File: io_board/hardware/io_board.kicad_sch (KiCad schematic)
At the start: 15 parts, among them J1 8bit_thing_bus_connector, J2 greenpak_i2c, J3 greenpak_i2c, J4 Micro_SD_Card_Det1, U1 SLG46826G, U2 W65C22, U3 74HCT164, U4 SLG46826G, U5 TLV73333PDBV

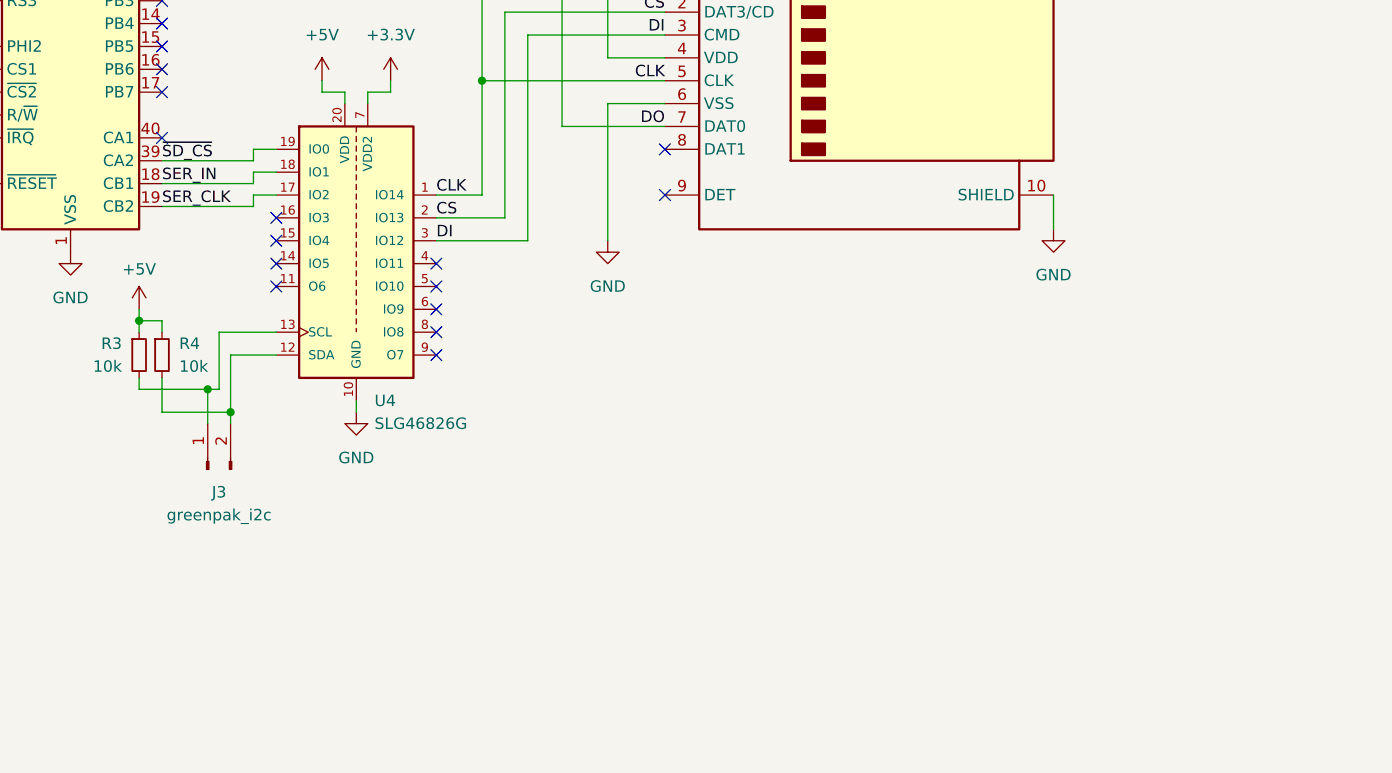
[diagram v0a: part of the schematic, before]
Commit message: Update IO board schematic and check in the necessary GreenPAK files
The io_spi_delay is built for a breadboard version using a '595 instead of a
'164, see the note in the schematic. It has an additional (further) delayed
clock line for the '595 register clock so we can shift and present the data in
the same PHI2 cycle.
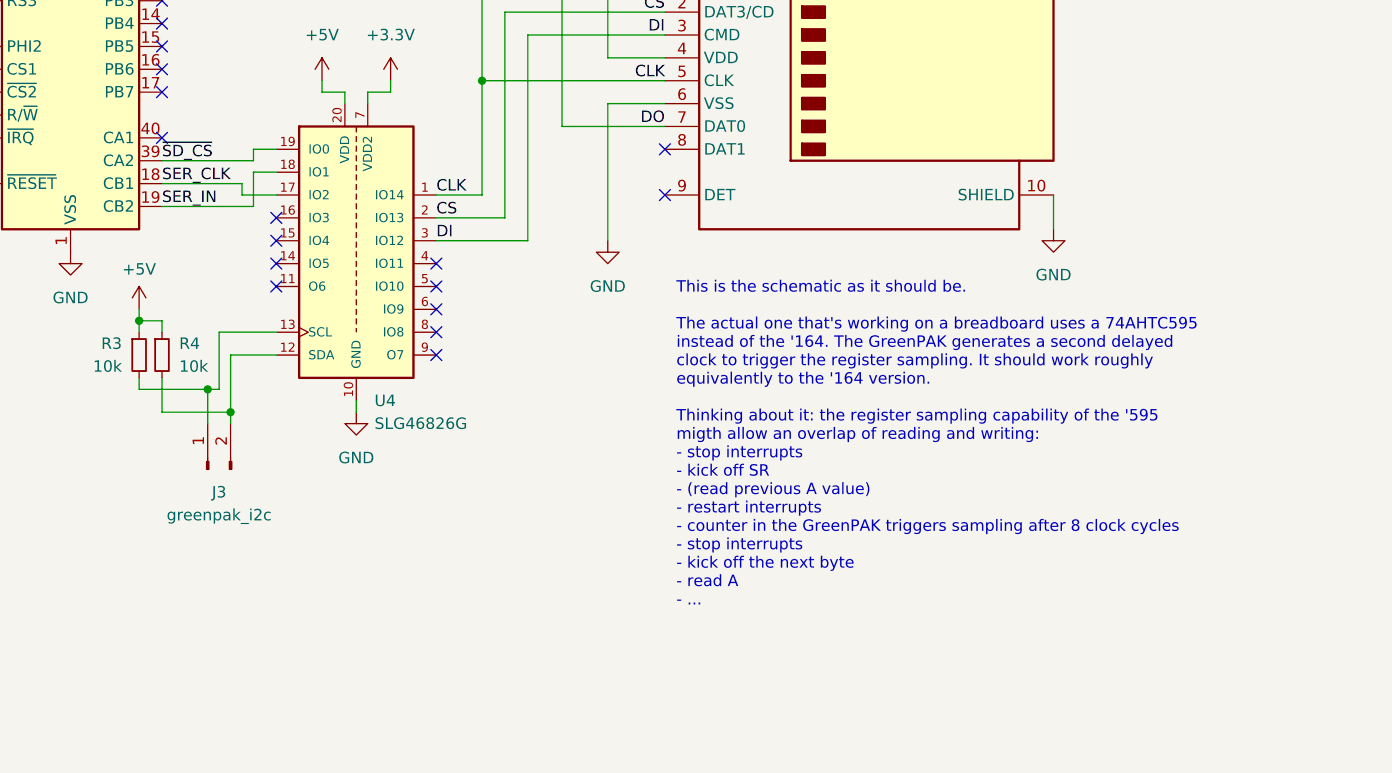
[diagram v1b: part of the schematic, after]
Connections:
- net SER_CLK: now also U2.18 (CB1); no longer U2.19 (CB2)
- net SER_IN: now also U2.19 (CB2); no longer U2.18 (CB1)
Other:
- note added: "This is the schematic as it should be. The actual one that's working on a breadboard uses a 74AHTC595 instead of the '164. The GreenPAK generates a second delayed clock to trigger the register sampling. It should work roughly equivalently to the '164 version. Thinking about it: the register sampling capability of the '595 migth allow an overlap of reading and writing: - stop interrupts - kick off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"
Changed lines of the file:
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@@
+	(wire
+		(pts
+			(xy 154.94 104.14) (xy 151.13 104.14)
+		)
+		(stroke
+			(width 0)
+			(type default)
+		)
+	)
 	(wire
 		(pts
@@
 	(wire
 		(pts
+			(xy 151.13 102.87) (xy 142.24 102.87)
+		)
+		(stroke
+			(width 0)
+			(type default)
+		)
+	)
+	(wire
+		(pts
 			(xy 53.34 138.43) (xy 53.34 139.7)
 		)
@@
 	(wire
 		(pts
-			(xy 142.24 102.87) (xy 152.4 102.87)
-		)
-		(stroke
-			(width 0)
-			(type default)
-		)
-	)
-	(wire
-		(pts
-			(xy 152.4 104.14) (xy 154.94 104.14)
-		)
-		(stroke
-			(width 0)
-			(type default)
-		)
-	)
-	(wire
-		(pts
 			(xy 220.98 44.45) (xy 220.98 40.64)
 		)
@@
 	(wire
 		(pts
-			(xy 152.4 105.41) (xy 152.4 104.14)
-		)
-		(stroke
-			(width 0)
-			(type default)
-		)
-	)
-	(wire
-		(pts
 			(xy 45.72 44.45) (xy 45.72 45.72)
 		)
@@
 	(wire
 		(pts
-			(xy 152.4 102.87) (xy 152.4 101.6)
+			(xy 151.13 104.14) (xy 151.13 102.87)
 		)
 		(stroke
@@
 	(wire
 		(pts
+			(xy 152.4 101.6) (xy 152.4 105.41)
+		)
+		(stroke
+			(width 0)
+			(type default)
+		)
+	)
+	(wire
+		(pts
 			(xy 167.64 92.71) (xy 165.1 92.71)
 		)
@@
 	(wire
 		(pts
-			(xy 152.4 101.6) (xy 154.94 101.6)
-		)
-		(stroke
-			(width 0)
-			(type default)
-		)
-	)
-	(wire
-		(pts
 			(xy 99.06 99.06) (xy 99.06 100.33)
 		)
@@
 	(wire
 		(pts
+			(xy 154.94 101.6) (xy 152.4 101.6)
+		)
+		(stroke
+			(width 0)
+			(type default)
+		)
+	)
+	(wire
+		(pts
 			(xy 182.88 86.36) (xy 182.88 109.22)
 		)
@@
 			(width 0)
 			(type default)
+		)
+	)
+	(text "This is the schematic as it should be.\n\nThe actual one that's working on a breadboard uses a 74AHTC595\ninstead of the '164. The GreenPAK generates a second delayed\nclock to trigger the register sampling. It should work roughly\nequivalently to the '164 version.\n\nThinking about it: the register sampling capability of the '595\nmigth allow an overlap of reading and writing:\n- stop interrupts\n- kick off SR\n- (read previous A value)\n- restart interrupts\n- counter in the GreenPAK triggers sampling after 8 clock cycles\n- stop interrupts\n- kick off the next byte\n- read A\n- ..."
+		(exclude_from_sim no)
+		(at 199.39 113.792 0)
+		(effects
+			(font
+				(size 1.27 1.27)
+			)
+			(justify left top)
 		)
 	)
@@
 	)
 	(label "SER_IN"
-		(at 142.24 102.87 0)
+		(at 142.24 105.41 0)
 		(fields_autoplaced yes)
 		(effects
@@
 		)
 	)
+	(label "SER_CLK"
+		(at 142.24 102.87 0)
+		(fields_autoplaced yes)
+		(effects
+			(font
+				(size 1.27 1.27)
+			)
+			(justify left bottom)
+		)
+	)
 	(label "CLK"
 		(at 121.92 87.63 180)
@@
 		(fields_autoplaced yes)
 		(effects
-			(font
-				(size 1.27 1.27)
-			)
-			(justify left bottom)
-		)
-	)
-	(label "SER_CLK"
-		(at 142.24 105.41 0)
-		(fields_autoplaced yes)
-		(effects

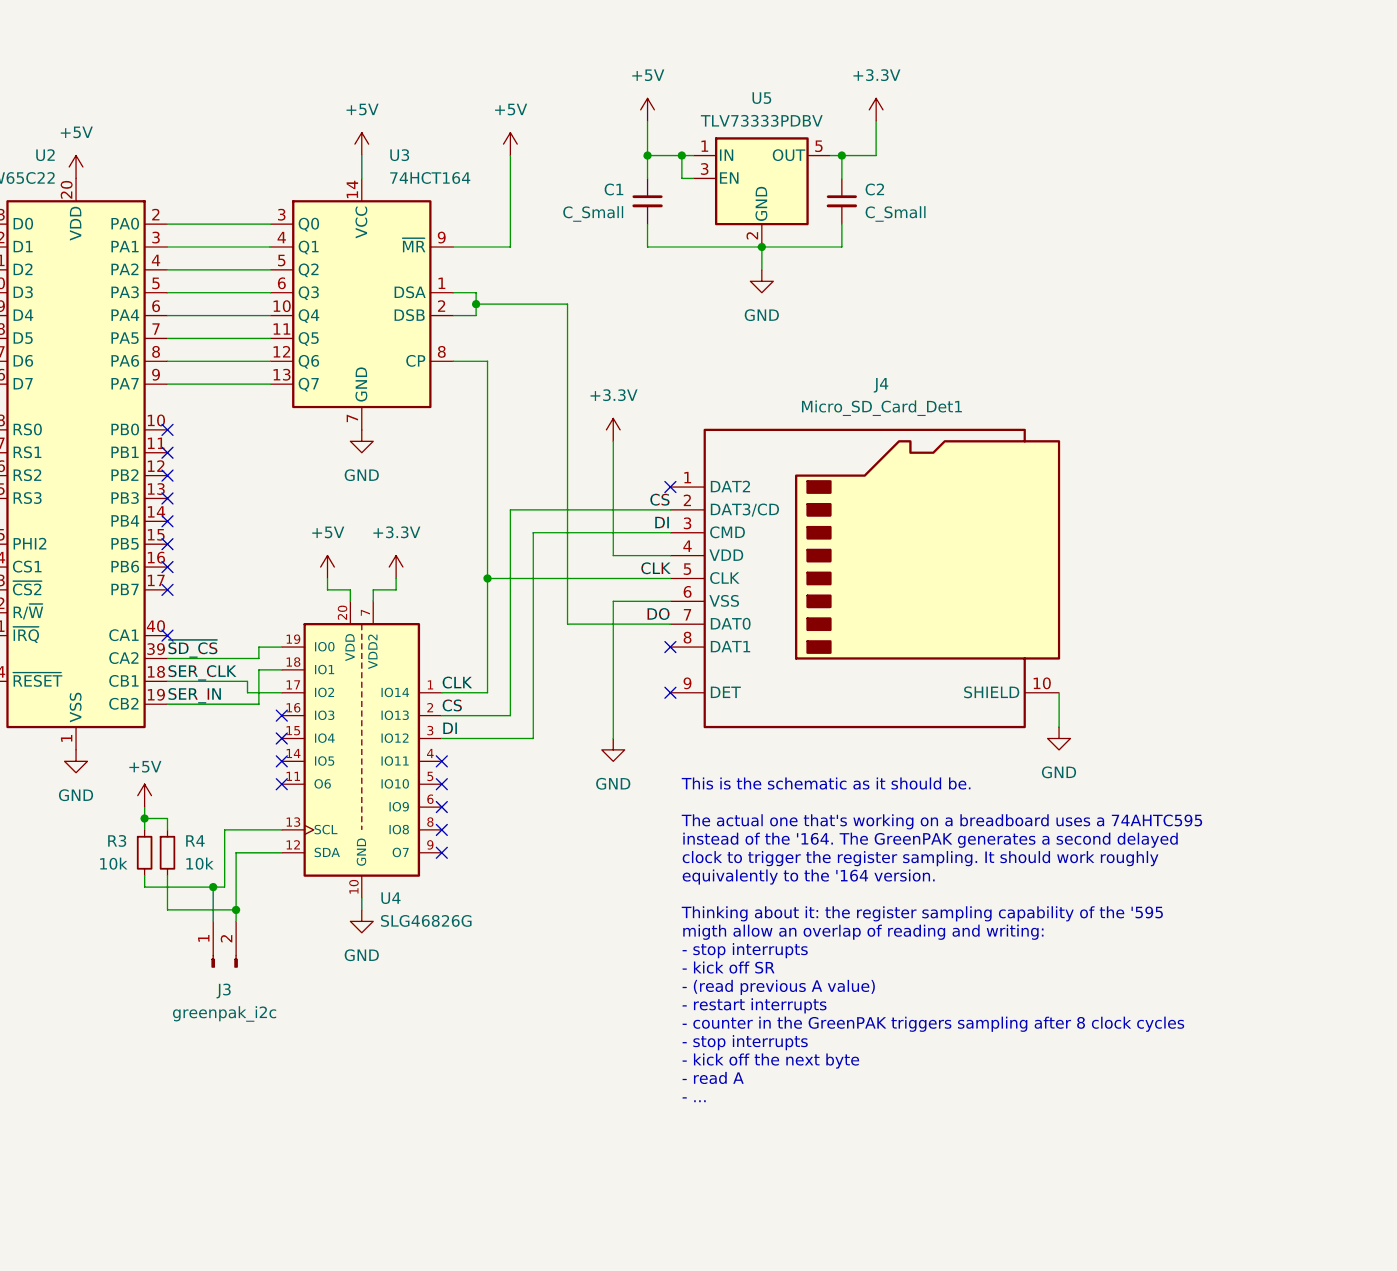
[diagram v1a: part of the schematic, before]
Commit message: IO board: update the schematic to use '595 for SD Card --> 65C22 comms
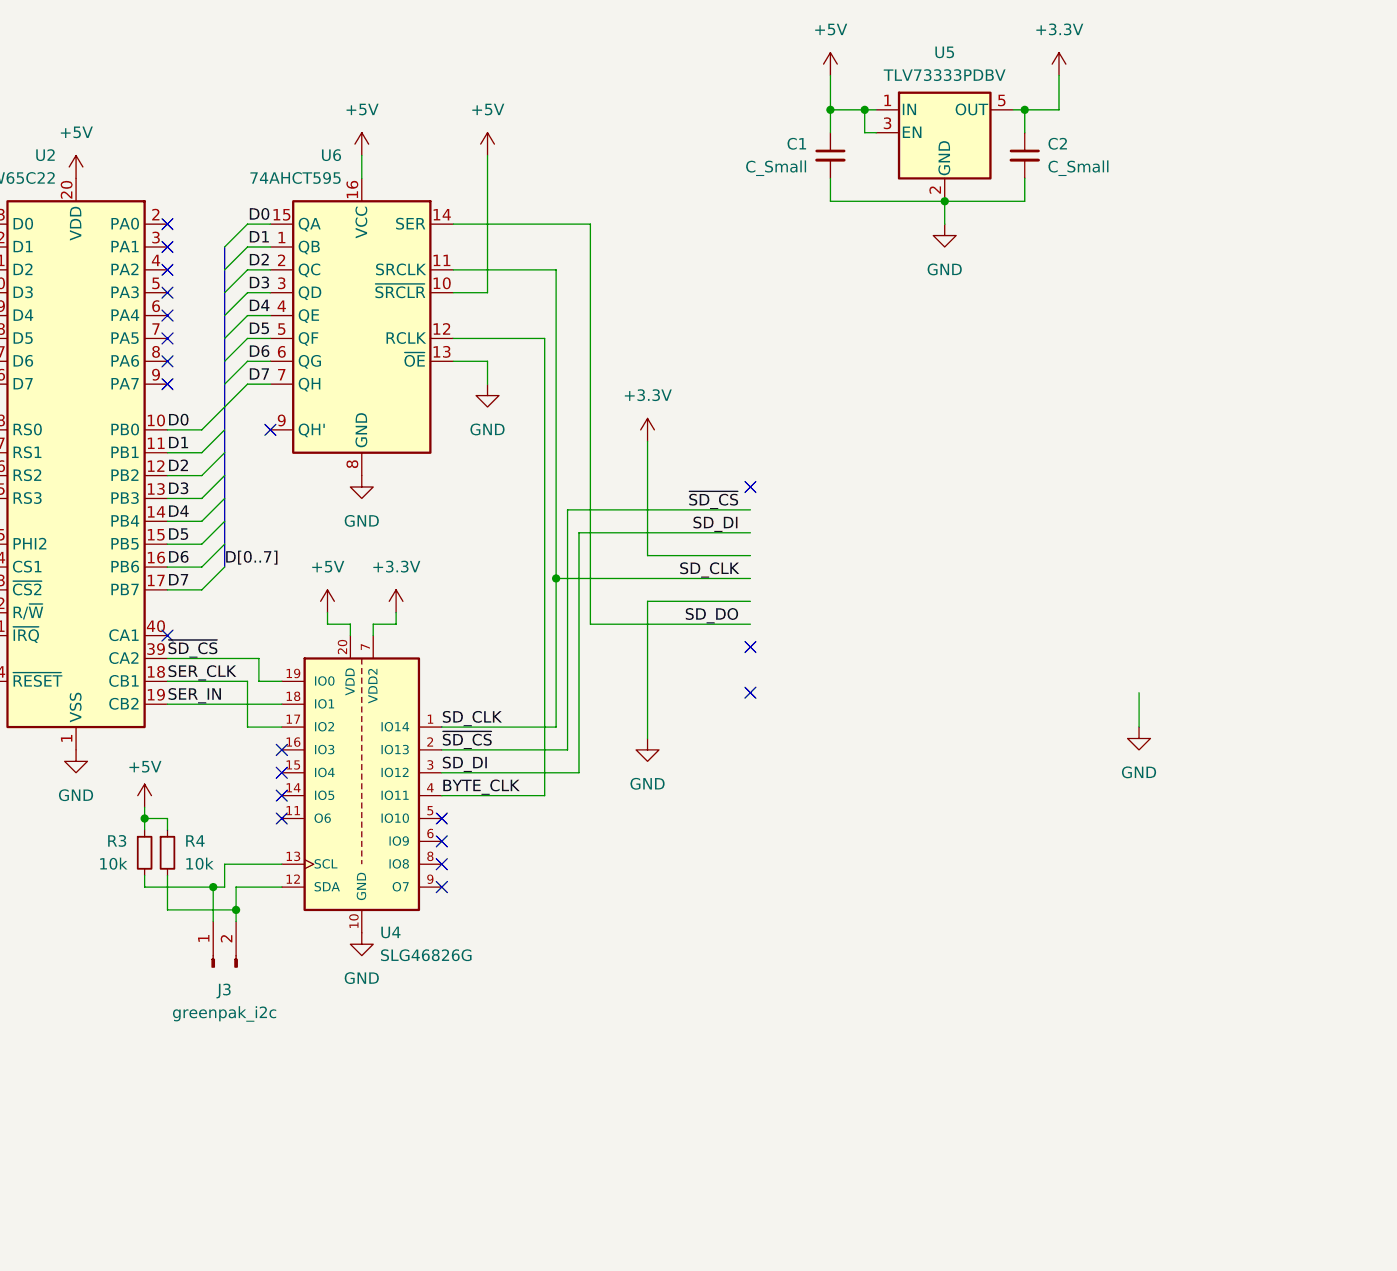
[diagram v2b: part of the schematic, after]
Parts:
- removed J4: Micro_SD_Card_Det1, symbol Connector:Micro_SD_Card_Det1
- removed U3: 74HCT164, symbol 74xx:74HCT164
- added U6: 74AHCT595, symbol 74xx:74AHCT595
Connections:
- net CS is gone; now on net ~{SD_CS}: U4.2 (IO13)
- net +5V: now also U6.10 (~{SRCLR}), U6.16 (VCC)
- net CLK: no longer U4.1 (IO14)
- net GND: now also U6.13 (~{OE}), U6.8 (GND)
- net D0: now reaches U2.10 (PB0)
- net D0: now also U6.15 (QA)
- net D1: now reaches U2.11 (PB1)
- net D1: now also U6.1 (QB)
- net D2: now reaches U2.12 (PB2)
- net D2: now also U6.2 (QC)
- net D3: now reaches U2.13 (PB3)
- net D3: now also U6.3 (QD)
- net D4: now reaches U2.14 (PB4)
- net D4: now also U6.4 (QE)
- net D5: now reaches U2.15 (PB5)
- net D5: now also U6.5 (QF)
- net D6: now reaches U2.16 (PB6)
- net D6: now also U6.6 (QG)
- net D7: now reaches U2.17 (PB7)
- net D7: now also U6.7 (QH)
- net BYTE_CLK: now reaches U4.4 (IO11)
- net BYTE_CLK: now also U6.12 (RCLK)
- net DI renamed SD_DI
- new net SD_CLK: U4.1 (IO14), U6.11 (SRCLK)
- new net SD_DO: U6.14 (SER)
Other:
- note removed: "This is the schematic as it should be. The actual one that's working on a breadboard uses a 74AHTC595 instead of the '164. The GreenPAK generates a second delayed clock to trigger the register sampling. It should work roughly equivalently to the '164 version. Thinking about it: the register sampling capability of the '595 migth allow an overlap of reading and writing: - stop interrupts - kick off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"
- moved on the sheet: C1, C2, U4, U5
